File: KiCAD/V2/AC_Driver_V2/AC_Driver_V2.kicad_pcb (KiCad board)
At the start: 2 copper layers, 130.8 x 85 mm, 126 parts, among them J1-120VAC1 Screw_Terminal_01x02, J2 USART6, J2-HVDC2 Screw_Terminal_01x02, J3 USB_B_Micro, J4 Conn_01x05_Pin, J5 USART2, J6 Receiver, Q1 2N3904, SW1 SW_Push, SW2 SW_SPDT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

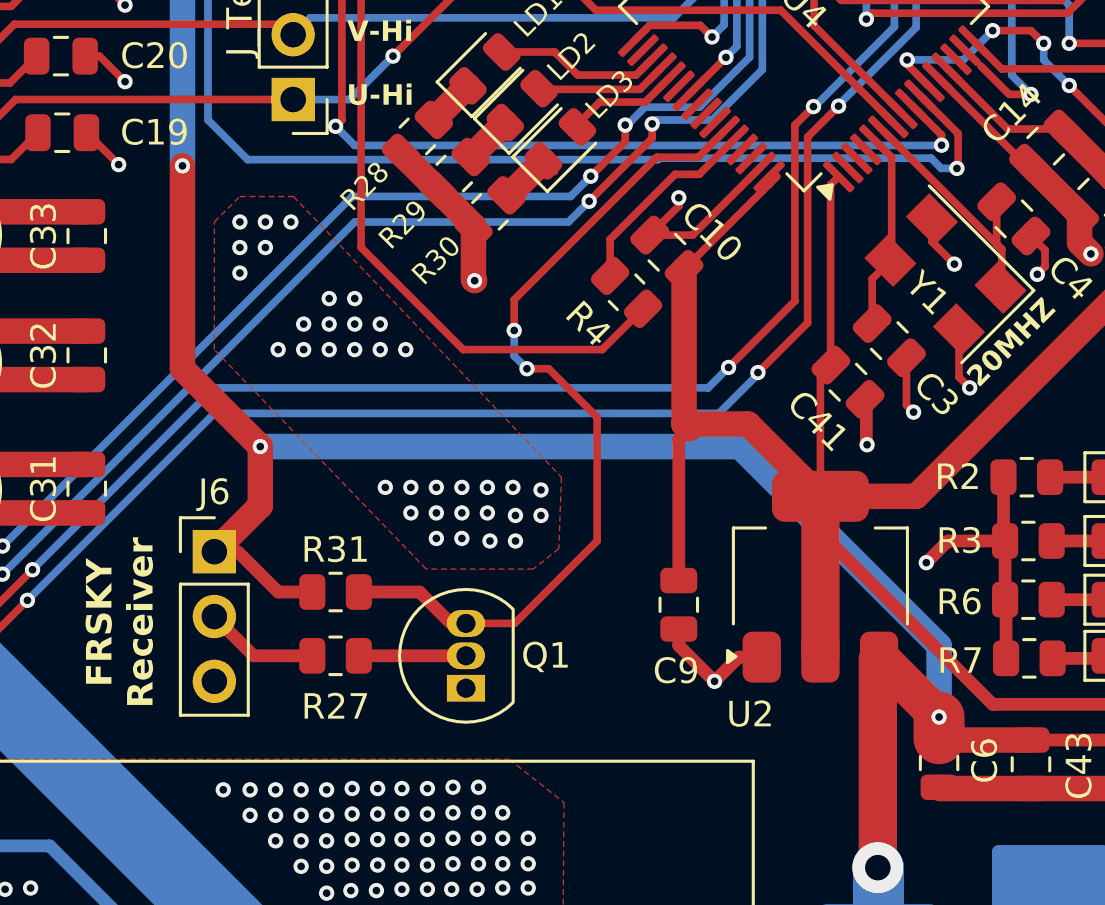
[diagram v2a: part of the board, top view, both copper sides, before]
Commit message: corrects receiver pins
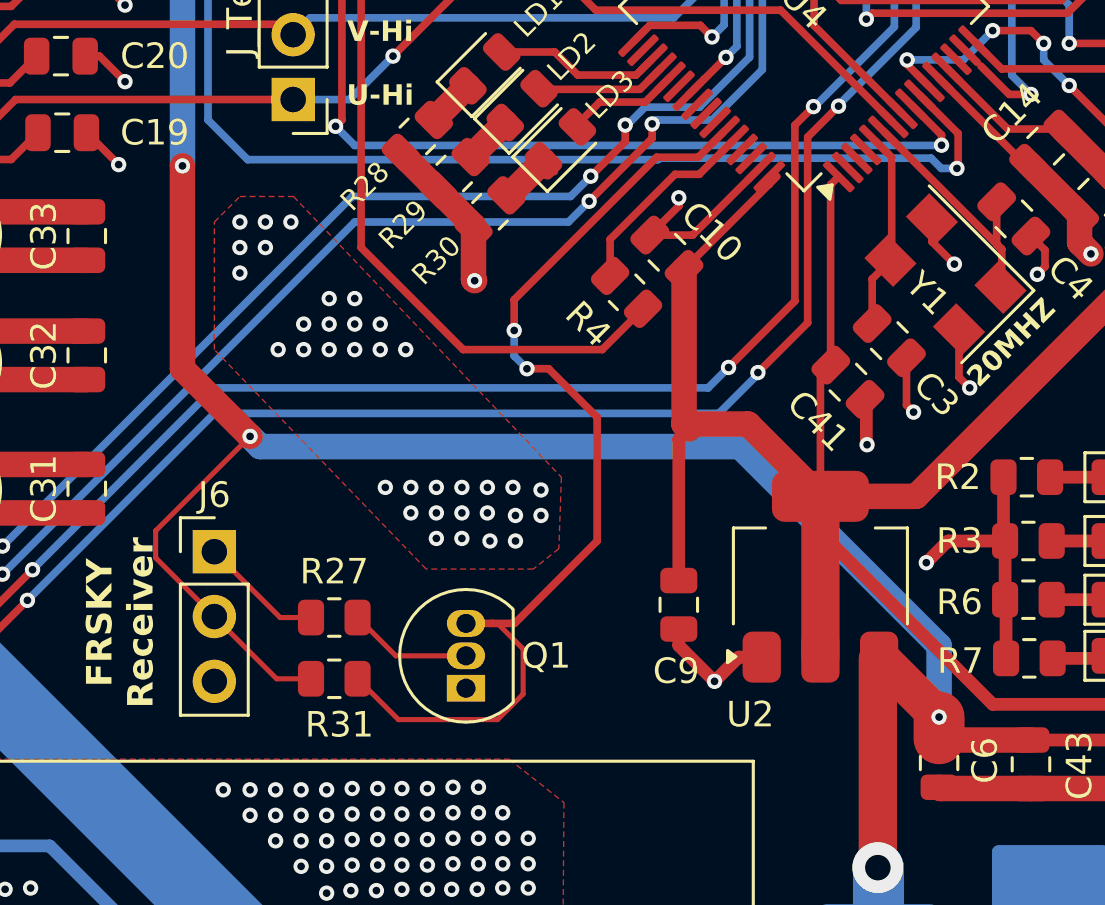
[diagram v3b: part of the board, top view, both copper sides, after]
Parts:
- moved R31 3.40 mm to (116.2, 80.4)
- moved R27 1.50 mm to (116.2, 78.0)
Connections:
- J6 pad 1: +5V -> Net-(J6-Pin_1)
- J6 pad 2: Net-(J6-Pin_2) -> +5V
- R27 pad 1: Net-(J6-Pin_2) -> Net-(J6-Pin_1)
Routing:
- net Net-(Q1-C): track 33.4 -> 41.3 mm
- net +5V: track 229.5 -> 234.5 mm
- net Net-(J6-Pin_1): track 0.00 -> 4.86 mm
- net Net-(J6-Pin_2): track 4.48 -> 0.00 mm
- net Net-(Q1-B): track 4.20 -> 4.87 mm
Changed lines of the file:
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@@
 	(net 117 "Net-(Q1-B)")
 	(net 118 "Net-(Q1-C)")
-	(net 119 "Net-(J6-Pin_2)")
+	(net 119 "Net-(J6-Pin_1)")
 	(net 120 "unconnected-(U4-PB6-Pad58)")
 	(footprint "Capacitor_SMD:C_0805_2012Metric"
@@
 	(footprint "Resistor_SMD:R_0805_2012Metric"
 		(layer "F.Cu")
-		(at 116.25 77)
+		(at 116.2 80.4)
 		(descr "Resistor SMD 0805 (2012 Metric), square (rectangular) end terminal, IPC_7351 nominal, (Body size source: IPC-SM-782 page 72, https://www.pcb-3d.com/wordpress/wp-content/uploads/ipc-sm-782a_amendment_1_and_2.pdf), generated with kicad-footprint-generator")
 		(tags "resistor")
 		(property "Reference" "R31"
-			(at 0 -1.65 0)
+			(at 0.2 1.8 0)
 			(layer "F.SilkS")
 			(effects
@@
 		(tags "Through hole pin header THT 1x03 2.54mm single row")
 		(property "Reference" "J6"
-			(at 0 -2.33 0)
+			(at 0 -2.22 0)
 			(layer "F.SilkS")
 			(effects
@@
 			(layers "*.Cu" "*.Mask")
 			(remove_unused_layers no)
-			(net 21 "+5V")
+			(net 119 "Net-(J6-Pin_1)")
 			(pinfunction "Pin_1")
 			(pintype "passive")
@@
 			(layers "*.Cu" "*.Mask")
 			(remove_unused_layers no)
-			(net 119 "Net-(J6-Pin_2)")
+			(net 21 "+5V")
 			(pinfunction "Pin_2")
 			(pintype "passive")
@@
 	(footprint "Resistor_SMD:R_0805_2012Metric"
 		(layer "F.Cu")
-		(at 116.25 79.5)
+		(at 116.2 78)
 		(descr "Resistor SMD 0805 (2012 Metric), square (rectangular) end terminal, IPC_7351 nominal, (Body size source: IPC-SM-782 page 72, https://www.pcb-3d.com/wordpress/wp-content/uploads/ipc-sm-782a_amendment_1_and_2.pdf), generated with kicad-footprint-generator")
 		(tags "resistor")
 		(property "Reference" "R27"
-			(at 0 2 0)
+			(at 0 -1.8 0)
 			(layer "F.SilkS")
 			(effects
@@
 			(layers "F.Cu" "F.Paste" "F.Mask")
 			(roundrect_rratio 0.243902)
-			(net 119 "Net-(J6-Pin_2)")
+			(net 119 "Net-(J6-Pin_1)")
 			(pintype "passive")
 		)
@@
 	)
 	(segment
+		(start 112.9 70.9)
+		(end 110.25 68.25)
+		(width 1)
+		(layer "F.Cu")
+		(net 21)
+	)
+	(segment
 		(start 152.3 81.6)
 		(end 151.1 82.8)
@@
 	)
 	(segment
-		(start 113.3 73.62)
-		(end 111.5 75.42)
-		(width 1)
-		(layer "F.Cu")
-		(net 21)
-	)
-	(segment
 		(start 126.685 36.75)
 		(end 125.825 35.89)
@@
 	)
 	(segment
+		(start 109.2 74.6)
+		(end 112.9 70.9)
+		(width 0.2)
+		(layer "F.Cu")
+		(net 21)
+	)
+	(segment
 		(start 143.5 82.8)
 		(end 139.95 82.8)
@@
 	)
 	(segment
-		(start 110.25 68.25)
-		(end 113.3 71.3)
-		(width 1)
-		(layer "F.Cu")
-		(net 21)
-	)
-	(segment
 		(start 139.9 81.9)
 		(end 137.55 79.55)
@@
 	)
 	(segment
-		(start 115.3375 77)
-		(end 114 77)
-		(width 0.5)
-		(layer "F.Cu")
-		(net 21)
-	)
-	(segment
 		(start 126.710589 42.249031)
 		(end 125.509099 43.450521)
@@
 	)
 	(segment
-		(start 113.3 71.3)
-		(end 113.3 73.62)
-		(width 1)
-		(layer "F.Cu")
-		(net 21)
-	)
-	(segment
 		(start 107.875 44.125)
 		(end 109.5 42.5)
@@
 	)
 	(segment
-		(start 114 77)
-		(end 112.42 75.42)
-		(width 0.5)
+		(start 115.2875 80.4)
+		(end 113.94 80.4)
+		(width 0.2)
 		(layer "F.Cu")
 		(net 21)
@@
 	)
 	(segment
-		(start 112.42 75.42)
-		(end 111.5 75.42)
-		(width 0.3)
-		(layer "F.Cu")
-		(net 21)
-	)
-	(segment
-		(start 110.25 60.3)
-		(end 110.25 68.25)
-		(width 1)
+		(start 109.2 75.66)
+		(end 109.2 74.6)
+		(width 0.2)
 		(layer "F.Cu")
 		(net 21)
@@
 	)
 	(segment
+		(start 111.5 77.96)
+		(end 109.2 75.66)
+		(width 0.2)
+		(layer "F.Cu")
+		(net 21)
+	)
+	(segment
+		(start 110.25 68.25)
+		(end 110.25 60.3)
+		(width 1)
+		(layer "F.Cu")
+		(net 21)
+	)
+	(segment
+		(start 113.94 80.4)
+		(end 111.5 77.96)
+		(width 0.2)
+		(layer "F.Cu")
+		(net 21)
+	)
+	(segment
 		(start 137.5 87.8)
 		(end 137.5 79.6)
@@
 	)
 	(via
-		(at 113.3 71.3)
+		(at 112.9 70.9)
 		(size 0.6)
 		(drill 0.3)
@@
 	)
 	(segment
-		(start 139.9 81.9)
+		(start 113.3 71.3)
+		(end 132.1 71.3)
+		(width 1)
+		(layer "B.Cu")
+		(net 21)
+	)
+	(segment
+		(start 132.1 71.3)
 		(end 139.9 79.1)
 		(width 1)
@@
 	)
 	(segment
-		(start 77 38)
-		(end 101.75 38)
+		(start 139.9 79.1)
+		(end 139.9 81.9)
 		(width 1)
 		(layer "B.Cu")
@@
 	)
 	(segment
-		(start 139.9 79.1)
-		(end 132.1 71.3)
+		(start 77 38)
+		(end 101.75 38)
 		(width 1)
 		(layer "B.Cu")
@@
 	)
 	(segment
-		(start 132.1 71.3)
-		(end 113.3 71.3)
-		(width 1)
-		(layer "B.Cu")
-		(net 21)
-	)
-	(segment
 		(start 154.578338 34.328338)
 		(end 154.578338 47.921662)
@@
 	)
 	(segment
+		(start 112.9 70.9)
+		(end 113.3 71.3)
+		(width 1)
+		(layer "B.Cu")
+		(net 21)
+	)
+	(segment
 		(start 110.25 60.3)
 		(end 110.25 46.5)
@@
 	(segment
 		(start 121.36 79.5)
-		(end 117.1625 79.5)
-		(width 0.5)
+		(end 118.6125 79.5)
+		(width 0.2)
 		(layer "F.Cu")
 		(net 117)
 	)
 	(segment
+		(start 118.6125 79.5)
+		(end 117.1125 78)
+		(width 0.2)
+		(layer "F.Cu")
+		(net 117)
+	)
+	(segment
+		(start 123.6 81)
+		(end 123.6 79.23)
+		(width 0.2)
+		(layer "F.Cu")
+		(net 118)
+	)
+	(segment
+		(start 123.6 79.23)
+		(end 122.6 78.23)
+		(width 0.2)
+		(layer "F.Cu")
+		(net 118)
+	)
+	(segment
+		(start 122.6 78.23)
+		(end 121.36 78.23)
+		(width 0.2)
+		(layer "F.Cu")
+		(net 118)
+	)
+	(segment
 		(start 126.5 75)
 		(end 123.27 78.23)
@@
 	)
 	(segment
+		(start 122.6 82)
+		(end 123.6 81)
+		(width 0.2)
+		(layer "F.Cu")
+		(net 118)
+	)
+	(segment
+		(start 122.4 78.23)
+		(end 121.36 78.23)
+		(width 0.3)
+		(layer "F.Cu")
+		(net 118)
+	)
+	(segment
 		(start 123.25 65.544307)
 		(end 128.831115 59.963192)
@@
 	)
 	(segment
+		(start 118.7125 82)
+		(end 122.6 82)
+		(width 0.2)
+		(layer "F.Cu")
+		(net 118)
+	)
+	(segment
 		(start 130.463191 59.963192)
 		(end 131.476851 58.949532)
@@
 	)
 	(segment
-		(start 123.27 78.23)
-		(end 121.36 78.23)
+		(start 124.6 68.25)
+		(end 126.5 70.15)
 		(width 0.3)
 		(layer "F.Cu")
@@
 	)
 	(segment
-		(start 124.6 68.25)
-		(end 126.5 70.15)
+		(start 123.27 78.23)
+		(end 122.4 78.23)
 		(width 0.3)
 		(layer "F.Cu")
@@
 	)
 	(segment
-		(start 119.54 77)
-		(end 117.1625 77)
-		(width 0.5)
+		(start 117.1125 80.4)
+		(end 118.7125 82)
+		(width 0.2)
 		(layer "F.Cu")
 		(net 118)
@@
 		(net 118)
 	)
-	(segment
-		(start 120.77 78.23)
-		(end 119.54 77)
-		(width 0.5)
-		(layer "F.Cu")
-		(net 118)
-	)
 	(via
 		(at 123.75 68.25)
@@
 	)
 	(segment
-		(start 113.04 79.5)
-		(end 111.5 77.96)
-		(width 0.5)
+		(start 115.2875 78)
+		(end 114.08 78)
+		(width 0.2)
 		(layer "F.Cu")
 		(net 119)
 	)
 	(segment
-		(start 115.3375 79.5)
-		(end 113.04 79.5)
-		(width 0.5)
+		(start 114.08 78)
+		(end 111.5 75.42)
+		(width 0.2)
 		(layer "F.Cu")
 		(net 119)

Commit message: sync
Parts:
- removed C3: 10p, Capacitor_SMD:C_0805_2012Metric
- C4: value 10p -> 10n
- J2: value USART6 -> Encoder
- moved C4 6.54 mm to (138.2, 67.0)
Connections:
- net /USART6_RX renamed /ChB
- net /USART6_TX renamed /ChA
- C4 pad 1: /HSE_OUT -> /HSE_IN
- C4 pad 2: GND -> /HSE_OUT
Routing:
- net GND: track 161.1 -> 156.5 mm, vias 721 -> 719
- net /HSE_OUT: track 10.6 -> 14.2 mm

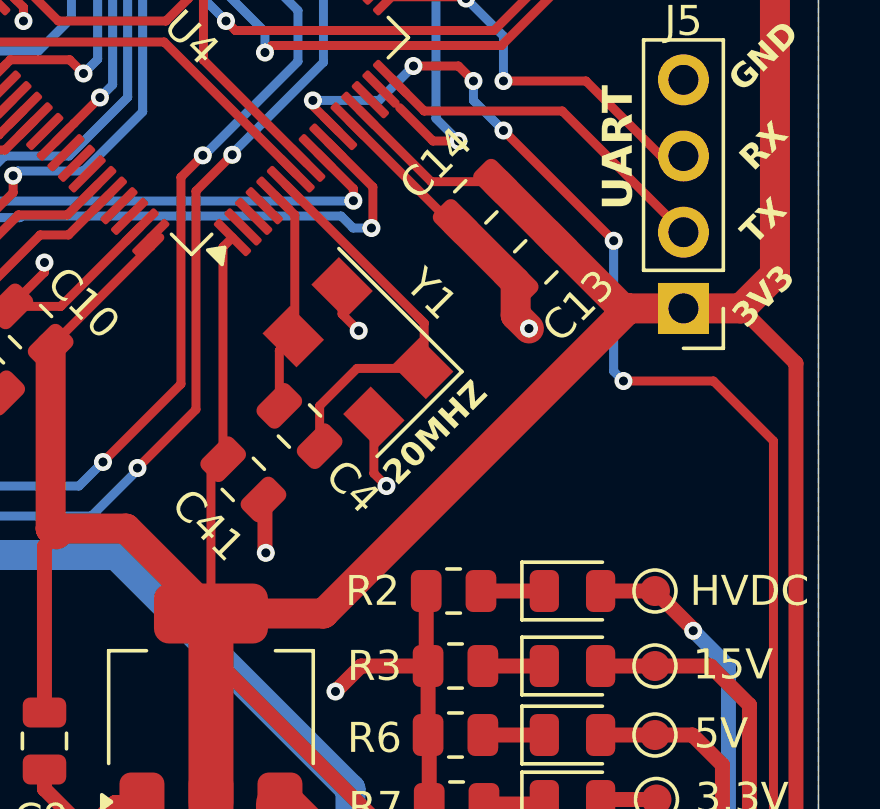
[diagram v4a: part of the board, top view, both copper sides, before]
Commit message: adds potentiameter to control the speed
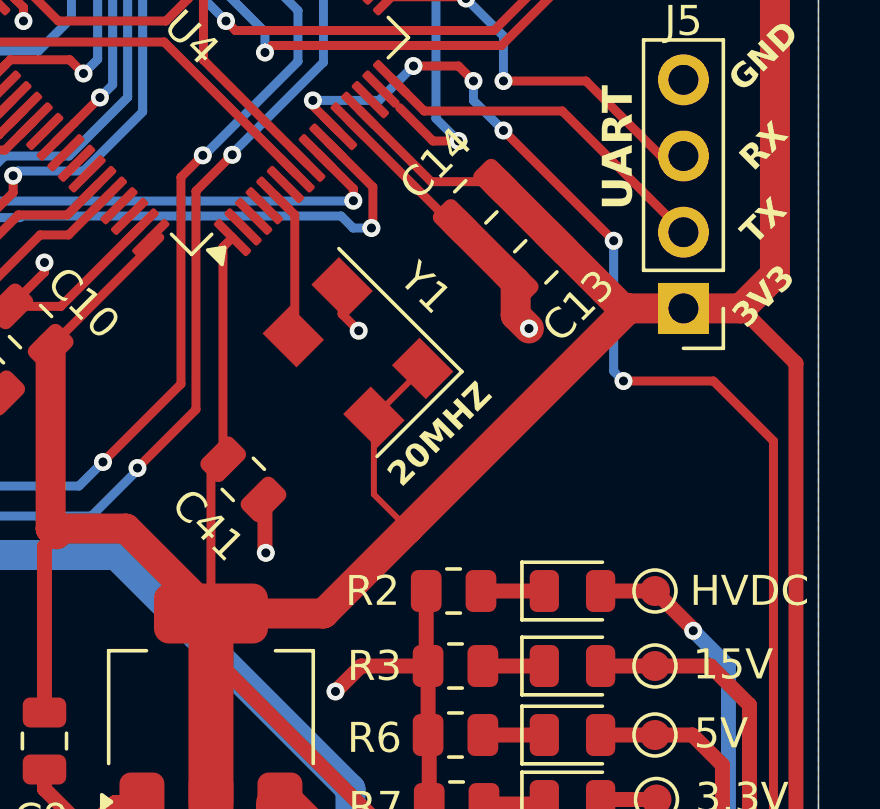
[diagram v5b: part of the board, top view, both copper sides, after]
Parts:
- removed C4: 10n, Capacitor_SMD:C_0805_2012Metric
- Y1: value 16MHZ_XTAL -> 20MHZ_OSC
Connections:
- U4 pad 6: /HSE_OUT -> unconnected-(U4-PH1-Pad6)
- Y1 pad 1: /HSE_OUT -> +3.3V
- Y1 pad 4: GND -> +3.3V
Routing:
- net /HSE_OUT: track 14.2 -> 0.00 mm
- net +3.3V: track 410.4 -> 417.6 mm
- net /HSE_IN: track 7.44 -> 4.94 mm
- net GND: track 156.5 -> 154.0 mm, vias 719 -> 718
